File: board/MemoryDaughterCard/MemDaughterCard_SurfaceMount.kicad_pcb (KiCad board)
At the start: 2 copper layers, 86.5 x 68.3 mm, 18 parts, among them IC1 HM628512LFP-7, IC2 HM628512LFP-7, IC3 HM628512LFP-7, IC4 HM628512LFP-7, IC5 HM628512LFP-7, IC6 HM628512LFP-7, IC7 HM628512LFP-7, IC8 HM628512LFP-7, J1 Conn_01x32, J2 Conn_01x24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

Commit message: Board V1.1G
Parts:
- IC2, IC3, IC6, IC7: moved to F.Cu
- J3: value E D C B A 9 8 7 6 5 4 3 2 1 0 -> Conn_02x15_Odd_Even
- J4: value A B -> Conn_01x15_Pin
- moved U1 61.2 mm to (151.4, 103.0), turned to 90 degrees
- moved C5 57.2 mm to (147.9, 95.4)
- moved IC5 53.6 mm to (114.7, 139.1), turned to 180 degrees
- moved IC4 53.3 mm to (178.7, 117.5), turned to 180 degrees
- moved C4 51.2 mm to (105.1, 127.0)
- moved IC6 45.4 mm to (133.8, 139.1), turned to 180 degrees
- moved J4 37.4 mm to (141.9, 95.6), turned to -90 degrees
- moved J3 34.3 mm to (141.9, 98.2), turned to -90 degrees
- moved C3 29.3 mm to (150.0, 127.0), turned to 180 degrees
- moved IC3 25.7 mm to (159.7, 117.5), turned to 180 degrees
- moved IC1 21.4 mm to (114.7, 117.5), turned to 180 degrees
- moved IC8 20.5 mm to (178.7, 139.1), turned to 180 degrees
- moved C1 19.2 mm to (105.1, 148.6), turned to 90 degrees
- moved IC2 18.0 mm to (133.8, 117.5), turned to 180 degrees
- moved IC7 8.54 mm to (159.7, 139.1), turned to 180 degrees
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- renumbered C6 to C4
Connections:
- U1 pad 4: Net-(IC3-~{CS}) -> Net-(IC4-~{CS})
- U1 pad 5: Net-(IC2-~{CS}) -> Net-(IC3-~{CS})
- U1 pad 6: Net-(IC1-~{CS}) -> Net-(IC2-~{CS})
- U1 pad 7: Net-(IC4-~{CS}) -> Net-(IC1-~{CS})
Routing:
- net RAMB2: track 97.1 -> 14.9 mm, vias 1 -> 0
- net RAMB3: track 92.4 -> 12.8 mm, vias 1 -> 0
- net A6: track 238.5 -> 164.2 mm, vias 5 -> 3
- net !RWB: track 138.4 -> 210.2 mm, vias 5 -> 1
- net A12: track 231.9 -> 165.6 mm, vias 5 -> 2
- net A8: track 130.0 -> 192.8 mm, vias 4 -> 0
- net A9: track 139.2 -> 198.6 mm, vias 4 -> 1
- net RWB: track 128.0 -> 187.2 mm, vias 5 -> 2
- net RAMB0: track 128.6 -> 187.0 mm, vias 4 -> 2
- net +5v: track 150.8 -> 201.2 mm
- net D3: track 127.3 -> 176.6 mm, vias 5 -> 2
- net A2: track 181.4 -> 226.4 mm, vias 5 -> 2
- net D4: track 131.1 -> 175.6 mm, vias 4 -> 2
- net T3: track 231.6 -> 188.6 mm, vias 5 -> 2
- net Net-(IC8-~{CS}): track 96.5 -> 53.5 mm
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- added copper zone on F.Cu, net GND
- removed copper zone on B.Cu, net +5v
- removed copper zone on F.Cu, net +5v
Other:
- board size 86.5 x 68.3 mm -> 88.9 x 67.3 mm

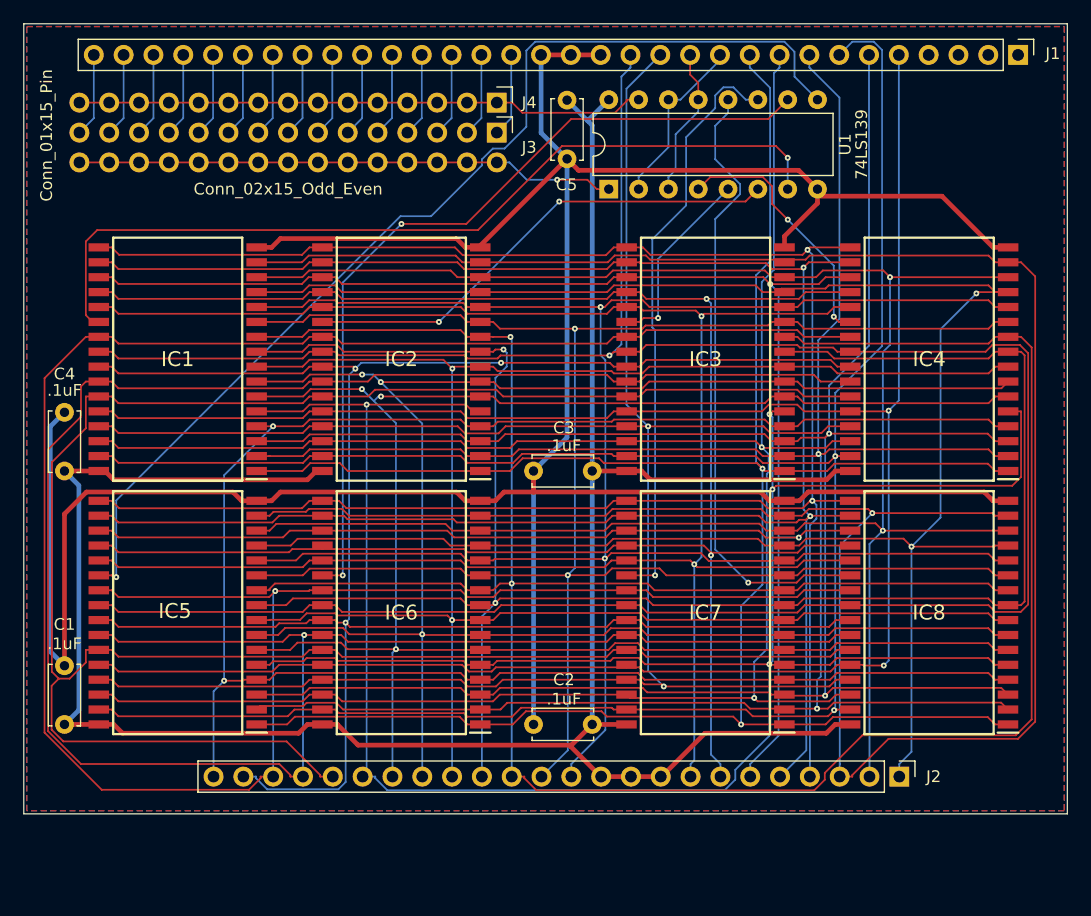
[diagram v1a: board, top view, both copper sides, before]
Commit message: V2.0 updates and new hydra breakout and counter cards.
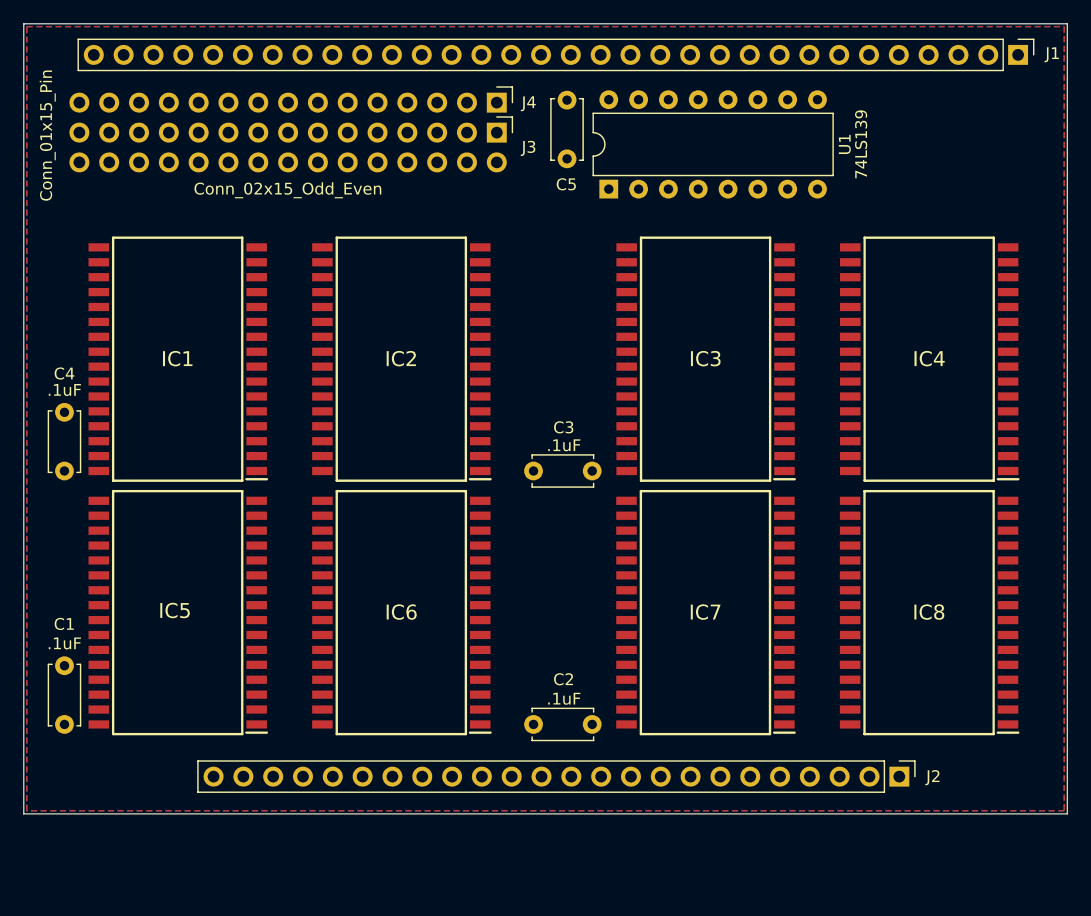
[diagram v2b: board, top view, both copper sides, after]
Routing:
- net GND: track 261.7 -> 0.00 mm
- net A2: track 226.4 -> 0.00 mm, vias 2 -> 0
- net D2: track 215.6 -> 0.00 mm, vias 1 -> 0
- net A7: track 211.7 -> 0.00 mm, vias 4 -> 0
- net !RWB: track 210.2 -> 0.00 mm, vias 1 -> 0
- net A10: track 205.1 -> 0.00 mm, vias 1 -> 0
- net +5v: track 201.2 -> 0.00 mm
- net A9: track 198.6 -> 0.00 mm, vias 1 -> 0
- net T2: track 193.6 -> 0.00 mm, vias 2 -> 0
- net A8: track 192.8 -> 0.00 mm
- net RAMB1: track 191.2 -> 0.00 mm, vias 2 -> 0
- net T0: track 189.7 -> 0.00 mm, vias 2 -> 0
- net T3: track 188.6 -> 0.00 mm, vias 2 -> 0
- net T1: track 187.3 -> 0.00 mm, vias 2 -> 0
- net RWB: track 187.2 -> 0.00 mm, vias 2 -> 0
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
